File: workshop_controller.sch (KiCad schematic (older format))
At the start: 14 parts, among them J1 Conn_02x10_Odd_Even, J2 Conn_02x10_Odd_Even, J3 AudioJack3, J4 Conn_01x08, SW1 SW_Push, SW2 SW_Push, U1 MPU-9250, U2 BME280, U3 MCP23S17_SS

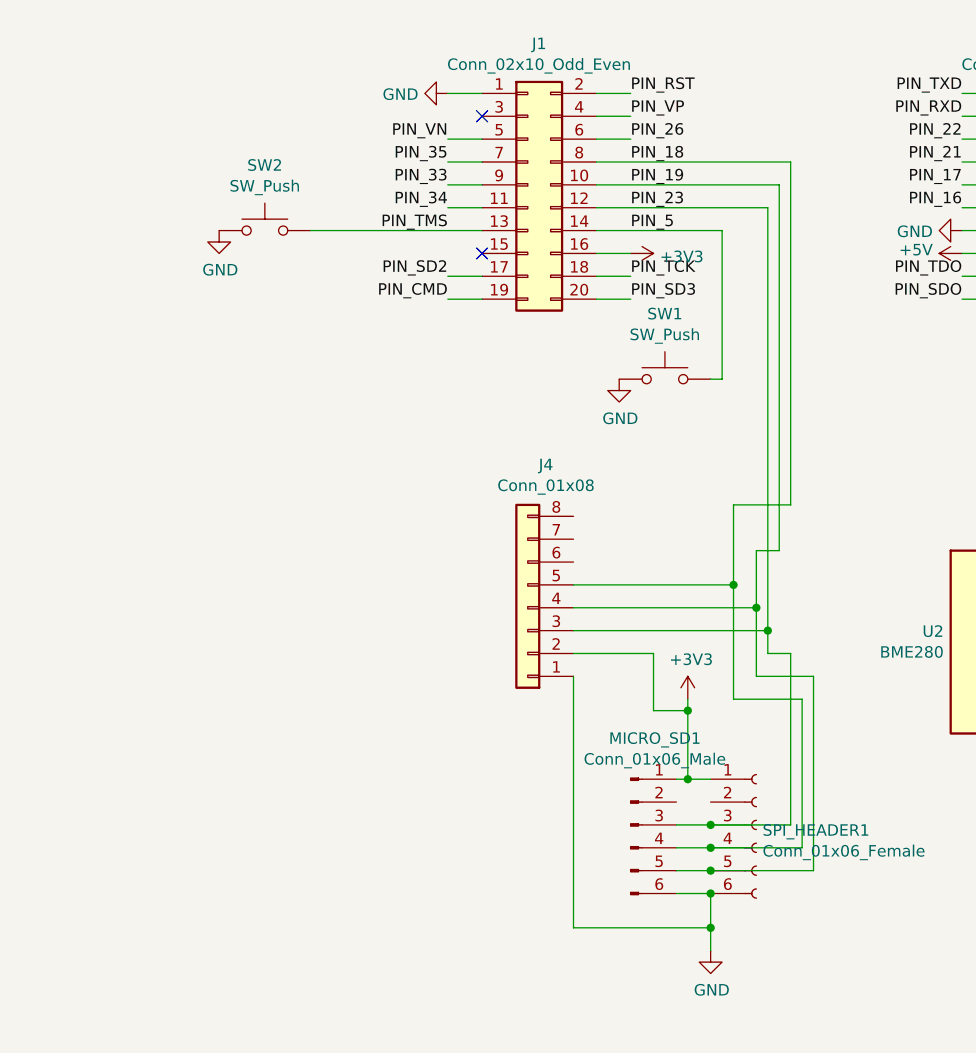
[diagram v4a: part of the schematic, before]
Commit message: Use correct symbol for FFC
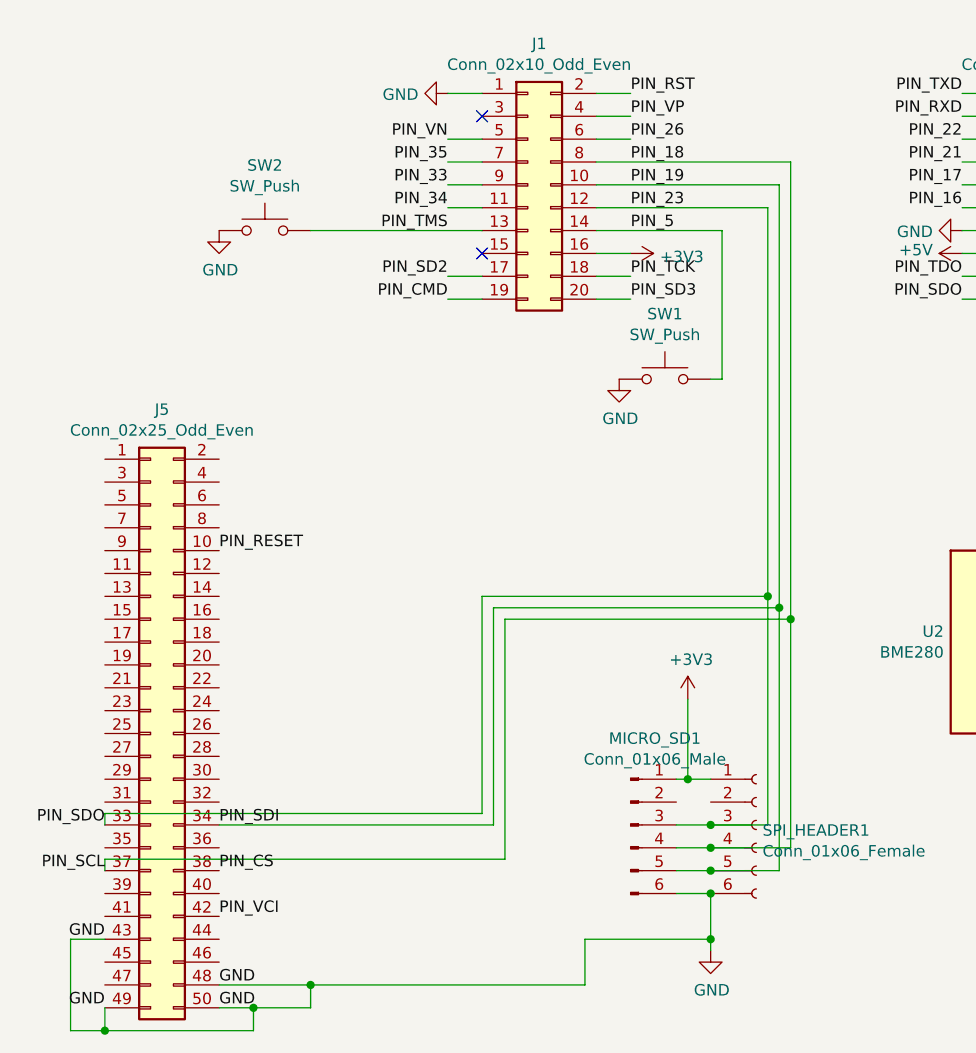
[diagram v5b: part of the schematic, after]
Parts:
- removed J4: Conn_01x08, Connector_FFC-FPC:Hirose_FH12-50S-0.5SH_1x50-1MP_P0.50mm_Horizontal, symbol Connector_Generic:Conn_01x08
- added J5: Conn_02x25_Odd_Even, Connector_FFC-FPC:Hirose_FH12-50S-0.5SH_1x50-1MP_P0.50mm_Horizontal, symbol Connector_Generic:Conn_02x25_Odd_Even
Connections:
- net PIN_SDO is gone; now on net PIN_23: J2.19 (Pin_19)
- net GND: now also J5.43 (Pin_43), J5.48 (Pin_48), J5.49 (Pin_49), J5.50 (Pin_50)
- net PIN_18: now also J5.37 (Pin_37)
- net PIN_19: now also J5.34 (Pin_34)
- net PIN_23: now also J5.33 (Pin_33)
- new net PIN_CS: J5.38 (Pin_38)
- new net PIN_RESET: J5.10 (Pin_10)
- new net PIN_VCI: J5.42 (Pin_42)
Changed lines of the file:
@@
 $EndComp
-Wire Wire Line
-	5850 4900 5850 3300
-Wire Wire Line
-	5050 3300 5850 3300
 Wire Wire Line
 	5050 3400 5800 3400
-Wire Wire Line
-	5900 3200 5900 4700
-Wire Wire Line
-	5900 4700 5650 4700
-Wire Wire Line
-	5050 3200 5900 3200
-Wire Wire Line
-	5800 5350 5900 5350
-Wire Wire Line
-	5750 4900 5750 5150
-Wire Wire Line
-	5750 5450 6000 5450
-Wire Wire Line
-	5750 4900 5850 4900
-Wire Wire Line
-	5650 4700 5650 5050
-Wire Wire Line
-	5650 5550 5950 5550
 $Comp
 L Connector:Conn_01x06_Male MICRO_SD1
@@
 	5400 6100 5550 6100
 Wire Wire Line
-	5900 6100 5900 5350
-Wire Wire Line
-	5400 6200 5550 6200
-Wire Wire Line
-	5950 6200 5950 5550
-Wire Wire Line
 	5400 6300 5550 6300
-Wire Wire Line
-	6000 6300 6000 5450
 $Comp
 L power:GND #PWR0106
@@
 	5400 6400 5550 6400
 Wire Wire Line
-	5450 5550 5450 5600
-Wire Wire Line
 	5450 5900 5400 5900
 $Comp
@@
 	1    0    0    -1
 $EndComp
-Connection ~ 5550 6100
-Wire Wire Line
-	5550 6100 5900 6100
-Connection ~ 5550 6200
-Wire Wire Line
-	5550 6200 5950 6200
-Connection ~ 5550 6300
-Wire Wire Line
-	5550 6300 6000 6300
 Connection ~ 5550 6400
 Wire Wire Line
@@
 Wire Wire Line
 	7700 6100 7700 6150
-Wire Wire Line
-	5550 6400 5550 6550
-$Comp
-L Connector_Generic:Conn_01x08 J4
-U 1 1 5CA73EBA
-P 4750 5150
-F 0 "J4" H 4670 4525 50  0000 C CNN
-F 1 "Conn_01x08" H 4670 4616 50  0000 C CNN
-F 2 "Connector_FFC-FPC:Hirose_FH12-50S-0.5SH_1x50-1MP_P0.50mm_Horizontal" H 4750 5150 50  0001 C CNN
-F 3 "~" H 4750 5150 50  0001 C CNN
-	1    4750 5150
-	-1   0    0    1
-$EndComp
-Wire Wire Line
-	4950 5050 5650 5050
-Connection ~ 5650 5050
-Wire Wire Line
-	5650 5050 5650 5550
-Wire Wire Line
-	4950 5150 5750 5150
-Connection ~ 5750 5150
-Wire Wire Line
-	5750 5150 5750 5450
-Wire Wire Line
-	4950 5250 5800 5250
-Wire Wire Line
-	5800 3400 5800 5250
-Connection ~ 5800 5250
-Wire Wire Line
-	5800 5250 5800 5350
-Wire Wire Line
-	4950 5350 5300 5350
-Wire Wire Line
-	5300 5350 5300 5600
-Wire Wire Line
-	5300 5600 5450 5600
-Connection ~ 5450 5600
-Wire Wire Line
-	5450 5600 5450 5900
-Wire Wire Line
-	4950 5450 4950 6550
-Wire Wire Line
-	4950 6550 5550 6550
-Connection ~ 5550 6550
-Wire Wire Line
-	5550 6550 5550 6650
+$Comp
+L Connector_Generic:Conn_02x25_Odd_Even J5
+U 1 1 5CA81708
+P 3100 5700
+F 0 "J5" H 3150 7117 50  0000 C CNN
+F 1 "Conn_02x25_Odd_Even" H 3150 7026 50  0000 C CNN
+F 2 "Connector_FFC-FPC:Hirose_FH12-50S-0.5SH_1x50-1MP_P0.50mm_Horizontal" H 3100 5700 50  0001 C CNN
+F 3 "~" H 3100 5700 50  0001 C CNN
+	1    3100 5700
+	1    0    0    -1
+$EndComp
+Wire Wire Line
+	5450 5550 5450 5900
+Wire Wire Line
+	5550 6400 5550 6600
+Text Label 3400 4900 0    50   ~ 0
+PIN_RESET
+Text Label 2900 6100 2    50   ~ 0
+PIN_SDO
+Text Label 3400 6100 0    50   ~ 0
+PIN_SDI
+Text Label 3400 6300 0    50   ~ 0
+PIN_CS
+Text Label 2900 6300 2    50   ~ 0
+PIN_SCL
+Text Label 2900 6600 2    50   ~ 0
+GND
+Text Label 3400 6800 0    50   ~ 0
+GND
+Text Label 3400 6900 0    50   ~ 0
+GND
+Text Label 2900 6900 2    50   ~ 0
+GND
+Text Label 3400 6500 0    50   ~ 0
+PIN_VCI
+Wire Wire Line
+	5050 3300 5850 3300
+Wire Wire Line
+	5800 6100 5550 6100
+Wire Wire Line
+	5800 3400 5800 5100
+Connection ~ 5550 6100
+Wire Wire Line
+	5400 6200 5550 6200
+Wire Wire Line
+	5550 6200 5900 6200
+Connection ~ 5550 6200
+Wire Wire Line
+	5050 3200 5900 3200
+Wire Wire Line
+	5900 3200 5900 5200
+Wire Wire Line
+	5850 6300 5550 6300
+Wire Wire Line
+	5850 3300 5850 5150
+Connection ~ 5550 6300
+Wire Wire Line
+	3400 6100 4600 6100
+Wire Wire Line
+	4600 6100 4600 5150
+Wire Wire Line
+	4600 5150 5850 5150
+Connection ~ 5850 5150
+Wire Wire Line
+	5850 5150 5850 6300
+Wire Wire Line
+	2900 6100 2900 6050
+Wire Wire Line
+	2900 6050 4550 6050
+Wire Wire Line
+	4550 6050 4550 5100
+Wire Wire Line
+	4550 5100 5800 5100
+Connection ~ 5800 5100
+Wire Wire Line
+	5800 5100 5800 6100
+Wire Wire Line
+	2900 6300 2900 6250
+Wire Wire Line
+	2900 6250 4650 6250
+Wire Wire Line
+	4650 6250 4650 5200
+Wire Wire Line
+	4650 5200 5900 5200
+Connection ~ 5900 5200
+Wire Wire Line
+	5900 5200 5900 6200
+Wire Wire Line
+	3400 6800 3800 6800
+Wire Wire Line
+	5000 6800 5000 6600
+Wire Wire Line
+	5000 6600 5550 6600
+Connection ~ 5550 6600
+Wire Wire Line
+	5550 6600 5550 6650
+Wire Wire Line
+	3400 6900 3550 6900
+Wire Wire Line
+	3800 6900 3800 6800
+Connection ~ 3800 6800
+Wire Wire Line
+	3800 6800 5000 6800
+Wire Wire Line
+	2900 6900 2900 7000
+Wire Wire Line
+	2900 7000 3550 7000
+Wire Wire Line
+	3550 7000 3550 6900
+Connection ~ 3550 6900
+Wire Wire Line
+	3550 6900 3800 6900
+Wire Wire Line
+	2900 6600 2750 6600
+Wire Wire Line
+	2750 6600 2750 7000
+Wire Wire Line
+	2750 7000 2900 7000
+Connection ~ 2900 7000
 $EndSCHEMATC

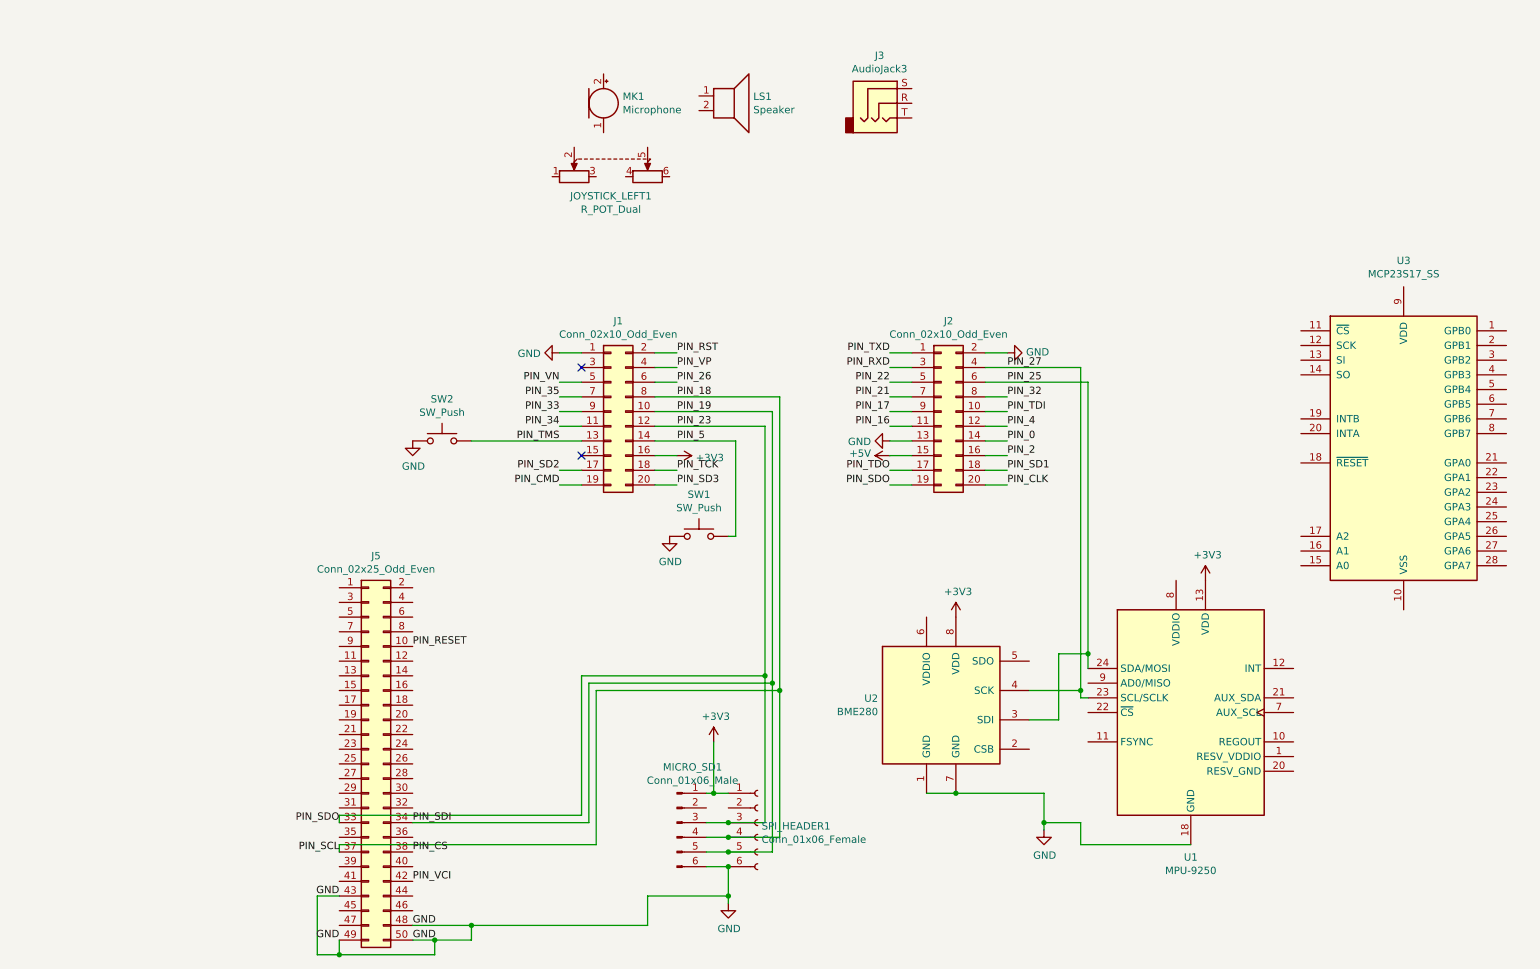
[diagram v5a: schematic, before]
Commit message: Connect mpu9250
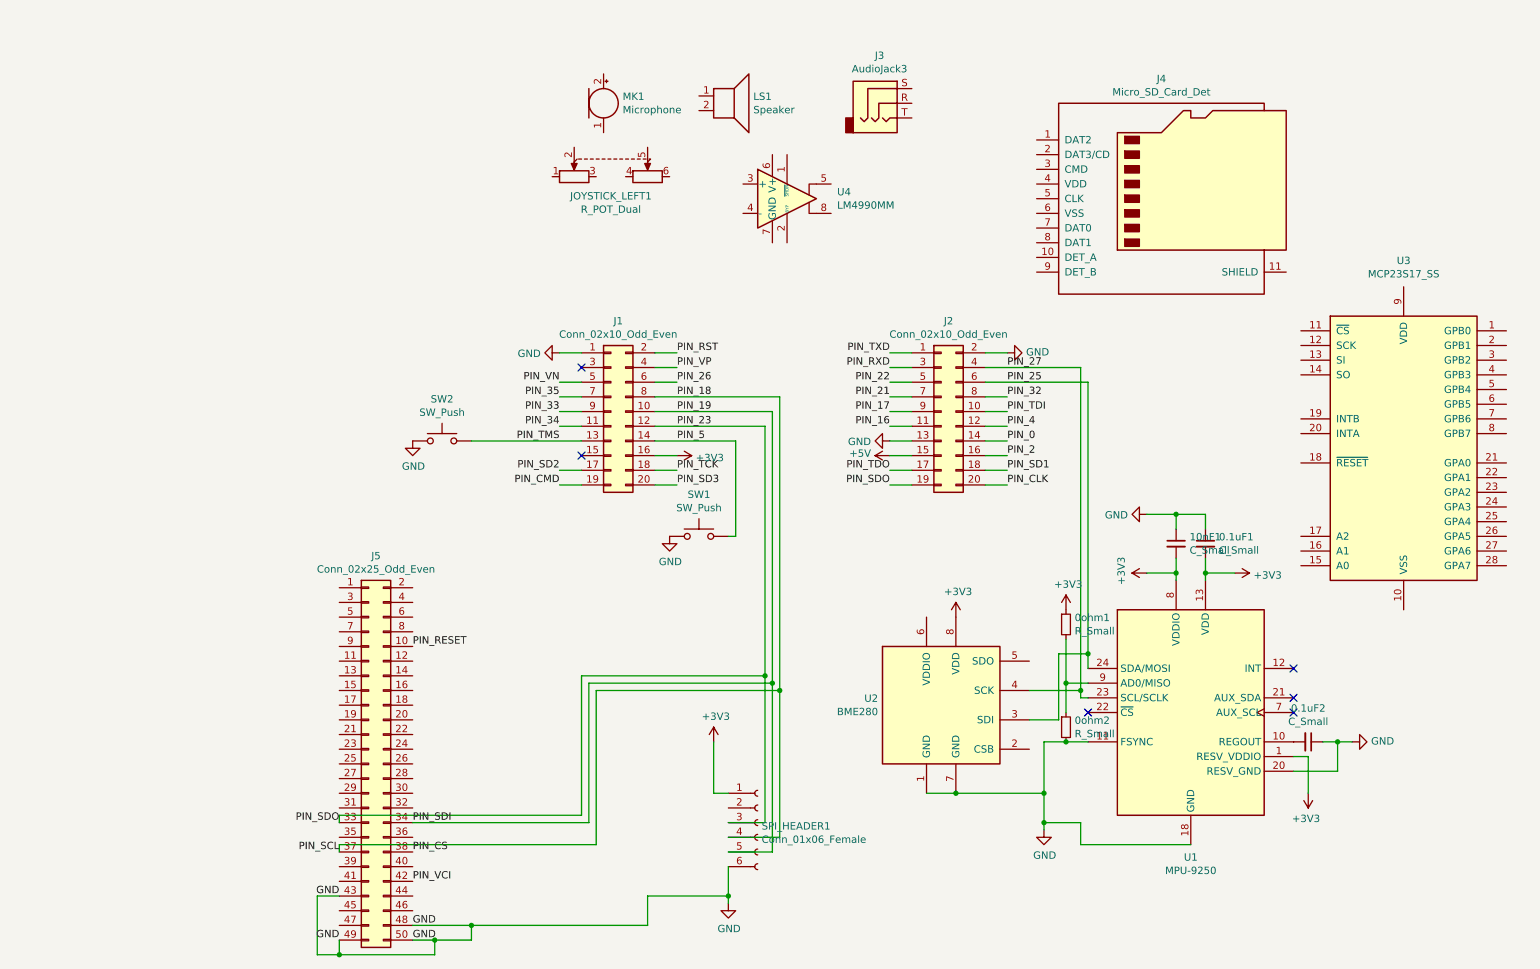
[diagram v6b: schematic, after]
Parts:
- removed MICRO_SD1: Conn_01x06_Male, Connector_PinHeader_2.54mm:PinHeader_1x06_P2.54mm_Vertical, symbol Connector:Conn_01x06_Male
- added 0.1uF1, 0.1uF2, 10nF1: C_Small, Capacitor_SMD:C_0603_1608Metric_Pad1.05x0.95mm_HandSolder, symbol Device:C_Small
- added 0ohm1, 0ohm2: R_Small, Resistor_SMD:R_0603_1608Metric_Pad1.05x0.95mm_HandSolder, symbol Device:R_Small
- added J4: Micro_SD_Card_Det, symbol Connector:Micro_SD_Card_Det
- added U4: LM4990MM, Package_SO:TSSOP-8_3x3mm_P0.65mm, symbol Amplifier_Audio:LM4990MM
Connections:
- net +3V3: now also U1.1 (RESV_VDDIO), U1.8 (VDDIO), 0.1uF1.2, 0ohm1.1, 10nF1.2
- net GND: now also U1.11 (FSYNC), U1.20 (RESV_GND), 0.1uF1.1, 0.1uF2.1, 0ohm2.2, 10nF1.1
- net at U1.10 (REGOUT): now also 0.1uF2.2
- net at U1.9 (AD0/MISO): now also 0ohm1.2, 0ohm2.1
- no-connect marks 2 -> 6
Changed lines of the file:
@@
 	5050 3400 5800 3400
-$Comp
-L Connector:Conn_01x06_Male MICRO_SD1
-U 1 1 5CA73B79
-P 5200 6100
-F 0 "MICRO_SD1" H 5306 6478 50  0000 C CNN
-F 1 "Conn_01x06_Male" H 5306 6387 50  0000 C CNN
-F 2 "Connector_PinHeader_2.54mm:PinHeader_1x06_P2.54mm_Vertical" H 5200 6100 50  0001 C CNN
-F 3 "~" H 5200 6100 50  0001 C CNN
-	1    5200 6100
-	1    0    0    -1
-$EndComp
-Wire Wire Line
-	5400 6100 5550 6100
-Wire Wire Line
-	5400 6300 5550 6300
 $Comp
 L power:GND #PWR0106
@@
 	1    0    0    -1
 $EndComp
-Wire Wire Line
-	5400 6400 5550 6400
-Wire Wire Line
-	5450 5900 5400 5900
 $Comp
 L power:+3V3 #PWR0108
 U 1 1 5CA89CBB
-P 8800 4450
-F 0 "#PWR0108" H 8800 4300 50  0001 C CNN
-F 1 "+3V3" H 8815 4623 50  0000 C CNN
-F 2 "" H 8800 4450 50  0001 C CNN
-F 3 "" H 8800 4450 50  0001 C CNN
-	1    8800 4450
-	1    0    0    -1
+P 8400 4400
+F 0 "#PWR0108" H 8400 4250 50  0001 C CNN
+F 1 "+3V3" H 8415 4573 50  0000 C CNN
+F 2 "" H 8400 4400 50  0001 C CNN
+F 3 "" H 8400 4400 50  0001 C CNN
+	1    8400 4400
+	0    -1   -1   0
 $EndComp
 $Comp
@@
 	1    0    0    -1
 $EndComp
-Connection ~ 5550 6400
 Wire Wire Line
 	5550 5900 5450 5900
-Connection ~ 5450 5900
 Wire Wire Line
 	8000 3100 8000 4950
@@
 Wire Wire Line
 	5800 3400 5800 5100
-Connection ~ 5550 6100
-Wire Wire Line
-	5400 6200 5550 6200
 Wire Wire Line
 	5550 6200 5900 6200
-Connection ~ 5550 6200
 Wire Wire Line
 	5050 3200 5900 3200
@@
 Wire Wire Line
 	5850 3300 5850 5150
-Connection ~ 5550 6300
 Wire Wire Line
 	3400 6100 4600 6100
@@
 	2750 7000 2900 7000
 Connection ~ 2900 7000
+$Comp
+L Amplifier_Audio:LM4990MM U4
+U 1 1 5CAD7DF6
+P 5950 1850
+F 0 "U4" H 6291 1896 50  0000 L CNN
+F 1 "LM4990MM" H 6291 1805 50  0000 L CNN
+F 2 "Package_SO:TSSOP-8_3x3mm_P0.65mm" H 5950 1850 50  0001 C CNN
+F 3 "http://www.ti.com/lit/ds/symlink/lm4990.pdf" H 5950 1850 50  0001 C CNN
+	1    5950 1850
+	1    0    0    -1
+$EndComp
+$Comp
+L Connector:Micro_SD_Card_Det J4
+U 1 1 5CA9E3F4
+P 8550 1850
+F 0 "J4" H 8500 2667 50  0000 C CNN
+F 1 "Micro_SD_Card_Det" H 8500 2576 50  0000 C CNN
+F 2 "" H 10600 2550 50  0001 C CNN
+F 3 "https://www.hirose.com/product/en/download_file/key_name/DM3/category/Catalog/doc_file_id/49662/?file_category_id=4&item_id=195&is_series=1" H 8550 1950 50  0001 C CNN
+	1    8550 1850
+	1    0    0    -1
+$EndComp
+$Comp
+L Device:C_Small 0.1uF1
+U 1 1 5CAAB507
+P 8800 4200
+F 0 "0.1uF1" H 8892 4246 50  0000 L CNN
+F 1 "C_Small" H 8892 4155 50  0000 L CNN
+F 2 "Capacitor_SMD:C_0603_1608Metric_Pad1.05x0.95mm_HandSolder" H 8800 4200 50  0001 C CNN
+F 3 "~" H 8800 4200 50  0001 C CNN
+	1    8800 4200
+	1    0    0    -1
+$EndComp
+$Comp
+L Device:C_Small 10nF1
+U 1 1 5CAAB5AB
+P 8600 4200
+F 0 "10nF1" H 8692 4246 50  0000 L CNN
+F 1 "C_Small" H 8692 4155 50  0000 L CNN
+F 2 "Capacitor_SMD:C_0603_1608Metric_Pad1.05x0.95mm_HandSolder" H 8600 4200 50  0001 C CNN
+F 3 "~" H 8600 4200 50  0001 C CNN
+	1    8600 4200
+	1    0    0    -1
+$EndComp
+$Comp
+L power:GND #PWR0113
+U 1 1 5CAAE80D
+P 8400 4000
+F 0 "#PWR0113" H 8400 3750 50  0001 C CNN
+F 1 "GND" V 8405 3872 50  0000 R CNN
+F 2 "" H 8400 4000 50  0001 C CNN
+F 3 "" H 8400 4000 50  0001 C CNN
+	1    8400 4000
+	0    1    1    0
+$EndComp
+Wire Wire Line
+	8600 4100 8600 4000
+Wire Wire Line
+	8600 4000 8400 4000
+Wire Wire Line
+	8800 4100 8800 4000
+Wire Wire Line
+	8800 4000 8600 4000
+Connection ~ 8600 4000
+Wire Wire Line
+	8800 4300 8800 4400
+Wire Wire Line
+	8600 4450 8600 4400
+Wire Wire Line
+	8600 4400 8400 4400
+Connection ~ 8600 4400
+Wire Wire Line
+	8600 4400 8600 4300
+$Comp
+L power:+3V3 #PWR0114
+U 1 1 5CAD51B3
+P 9000 4400
+F 0 "#PWR0114" H 9000 4250 50  0001 C CNN
+F 1 "+3V3" V 9015 4528 50  0000 L CNN
+F 2 "" H 9000 4400 50  0001 C CNN
+F 3 "" H 9000 4400 50  0001 C CNN
+	1    9000 4400
+	0    1    1    0
+$EndComp
+Wire Wire Line
+	8800 4400 9000 4400
+Connection ~ 8800 4400
+Wire Wire Line
+	8800 4400 8800 4450
+$Comp
+L Device:C_Small 0.1uF2
+U 1 1 5CAD8E6E
+P 9500 5550
+F 0 "0.1uF2" V 9271 5550 50  0000 C CNN
+F 1 "C_Small" V 9362 5550 50  0000 C CNN
+F 2 "Capacitor_SMD:C_0603_1608Metric_Pad1.05x0.95mm_HandSolder" H 9500 5550 50  0001 C CNN
+F 3 "~" H 9500 5550 50  0001 C CNN
+	1    9500 5550
+	0    1    1    0
+$EndComp
+$Comp
+L power:GND #PWR0115
+U 1 1 5CAD8F77
+P 9800 5550
+F 0 "#PWR0115" H 9800 5300 50  0001 C CNN
+F 1 "GND" V 9805 5422 50  0000 R CNN
+F 2 "" H 9800 5550 50  0001 C CNN
+F 3 "" H 9800 5550 50  0001 C CNN
+	1    9800 5550
+	0    -1   -1   0
+$EndComp
+Wire Wire Line
+	9600 5550 9700 5550
+Wire Wire Line
+	9400 5750 9700 5750
+Wire Wire Line
+	9700 5750 9700 5550
+Connection ~ 9700 5550
+Wire Wire Line
+	9700 5550 9800 5550
+Wire Wire Line
+	8000 5550 7850 5550
+Wire Wire Line
+	7700 5550 7700 5900
+Connection ~ 7700 5900
+$Comp
+L power:+3V3 #PWR0116
+U 1 1 5CAF1926
+P 9500 5900
+F 0 "#PWR0116" H 9500 5750 50  0001 C CNN
+F 1 "+3V3" H 9515 6073 50  0000 C CNN
+F 2 "" H 9500 5900 50  0001 C CNN
+F 3 "" H 9500 5900 50  0001 C CNN
+	1    9500 5900
+	-1   0    0    1
+$EndComp
+Wire Wire Line
+	9400 5650 9500 5650
+Wire Wire Line
+	9500 5650 9500 5900
+NoConn ~ 9400 5250
+NoConn ~ 9400 5350
+NoConn ~ 9400 5050
+NoConn ~ 8000 5350
+$Comp
+L Device:R_Small 0ohm1
+U 1 1 5CB08528
+P 7850 4750
+F 0 "0ohm1" H 7909 4796 50  0000 L CNN
+F 1 "R_Small" H 7909 4705 50  0000 L CNN
+F 2 "Resistor_SMD:R_0603_1608Metric_Pad1.05x0.95mm_HandSolder" H 7850 4750 50  0001 C CNN
+F 3 "~" H 7850 4750 50  0001 C CNN
+	1    7850 4750
+	1    0    0    -1
+$EndComp
+$Comp
+L Device:R_Small 0ohm2
+U 1 1 5CB085A3
+P 7850 5450
+F 0 "0ohm2" H 7909 5496 50  0000 L CNN
+F 1 "R_Small" H 7909 5405 50  0000 L CNN
+F 2 "Resistor_SMD:R_0603_1608Metric_Pad1.05x0.95mm_HandSolder" H 7850 5450 50  0001 C CNN
+F 3 "~" H 7850 5450 50  0001 C CNN
+	1    7850 5450
+	1    0    0    -1
+$EndComp
+Wire Wire Line
+	8000 5150 7850 5150
+Wire Wire Line
+	7850 5150 7850 4850
+$Comp
+L power:+3V3 #PWR0117
+U 1 1 5CB0C3C5
+P 7850 4650
+F 0 "#PWR0117" H 7850 4500 50  0001 C CNN
+F 1 "+3V3" H 7865 4823 50  0000 C CNN
+F 2 "" H 7850 4650 50  0001 C CNN
+F 3 "" H 7850 4650 50  0001 C CNN
+	1    7850 4650
+	1    0    0    -1
+$EndComp
+Connection ~ 7850 5550
+Wire Wire Line
+	7850 5550 7700 5550
+Wire Wire Line
+	7850 5350 7850 5150
+Connection ~ 7850 5150
 $EndSCHEMATC
